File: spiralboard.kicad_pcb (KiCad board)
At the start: 2 copper layers, 88.5 x 100 mm, 85 parts, among them J1 Conn_01x05_Pin, J2 Conn_01x02_Pin, U1 ESP-12F, U2 AMS1117-3.3

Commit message: update
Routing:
- net +3V3: track 96.5 -> 95.2 mm
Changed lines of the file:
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@@
   (segment (start 151.13 133.572) (end 150.654 133.096) (width 0.5) (layer "B.Cu") (net 1))
   (segment (start 176.895 126.619) (end 176.895 126.762) (width 0.5) (layer "B.Cu") (net 1))
-  (segment (start 145.454 124.841) (end 146.304 124.841) (width 0.5) (layer "B.Cu") (net 1))
   (segment (start 176.895 126.619) (end 177.165 126.619) (width 0.5) (layer "B.Cu") (net 1))
   (segment (start 178.816 122.047) (end 172.660918 122.047) (width 0.5) (layer "B.Cu") (net 1))
   (segment (start 150.654 128.365) (end 152.8025 126.2165) (width 0.5) (layer "B.Cu") (net 1))
-  (segment (start 147.182 123.963) (end 147.182 119.761) (width 0.5) (layer "B.Cu") (net 1))
   (segment (start 148.942082 136.486) (end 151.13 134.298082) (width 0.5) (layer "B.Cu") (net 1))
-  (segment (start 147.182 120.534) (end 147.182 119.761) (width 0.5) (layer "B.Cu") (net 1))
-  (segment (start 148.717 116.646864) (end 148.717 113.767) (width 0.5) (layer "B.Cu") (net 1))
   (segment (start 145.454 124.841) (end 145.454 134.972082) (width 0.5) (layer "B.Cu") (net 1))
+  (segment (start 145.454 124.841) (end 146.5795 123.7155) (width 0.5) (layer "B.Cu") (net 1))
   (segment (start 175.26 128.397) (end 175.26 129.286) (width 0.5) (layer "B.Cu") (net 1))
   (segment (start 152.8025 126.2165) (end 152.8025 124.079) (width 0.5) (layer "B.Cu") (net 1))
   (segment (start 152.8025 124.079) (end 155.935 124.079) (width 0.5) (layer "B.Cu") (net 1))
   (segment (start 179.705 124.079) (end 179.705 122.936) (width 0.5) (layer "B.Cu") (net 1))
-  (segment (start 147.182 118.181864) (end 148.717 116.646864) (width 0.5) (layer "B.Cu") (net 1))
   (segment (start 145.454 124.841) (end 143.748 124.841) (width 0.5) (layer "B.Cu") (net 1))
   (segment (start 145.454 134.972082) (end 146.967918 136.486) (width 0.5) (layer "B.Cu") (net 1))
   (segment (start 176.895 130.921) (end 176.895 131.953) (width 0.5) (layer "B.Cu") (net 1))
   (segment (start 150.654 133.096) (end 150.654 128.365) (width 0.5) (layer "B.Cu") (net 1))
+  (segment (start 148.717 116.646864) (end 148.717 113.767) (width 0.5) (layer "B.Cu") (net 1))
+  (segment (start 146.5795 119.761) (end 146.5795 118.784364) (width 0.5) (layer "B.Cu") (net 1))
   (segment (start 175.26 129.286) (end 176.895 130.921) (width 0.5) (layer "B.Cu") (net 1))
   (segment (start 176.895 126.762) (end 175.26 128.397) (width 0.5) (layer "B.Cu") (net 1))
-  (segment (start 146.304 124.841) (end 147.182 123.963) (width 0.5) (layer "B.Cu") (net 1))
   (segment (start 148.717 107.467) (end 148.717 113.767) (width 0.5) (layer "B.Cu") (net 1))
   (segment (start 152.8025 121.92) (end 152.8025 124.079) (width 0.5) (layer "B.Cu") (net 1))
-  (segment (start 147.182 119.761) (end 147.182 118.181864) (width 0.5) (layer "B.Cu") (net 1))
   (segment (start 179.705 122.936) (end 178.816 122.047) (width 0.5) (layer "B.Cu") (net 1))
+  (segment (start 146.5795 123.7155) (end 146.5795 119.761) (width 0.5) (layer "B.Cu") (net 1))
+  (segment (start 146.5795 118.784364) (end 148.717 116.646864) (width 0.5) (layer "B.Cu") (net 1))
   (via (at 181.61 120.396) (size 0.8) (drill 0.4) (layers "F.Cu" "B.Cu") (free) (net 2))
   (via (at 152.527 82.55) (size 0.8) (drill 0.4) (layers "F.Cu" "B.Cu") (free) (net 2))
@@
   (segment (start 156.906 75.504) (end 155.702 76.708) (width 0.5) (layer "F.Cu") (net 3))
   (segment (start 145.303467 115.759607) (end 147.697607 115.759607) (width 0.5) (layer "F.Cu") (net 3))
-  (segment (start 169.093747 112.272253) (end 169.164 112.202) (width 0.5) (layer "F.Cu") (net 3))
   (segment (start 192.404832 84.417916) (end 192.404832 81.849168) (width 0.5) (layer "F.Cu") (net 3))
   (segment (start 158.000249 74.729751) (end 157.226 75.504) (width 0.5) (layer "F.Cu") (net 3))

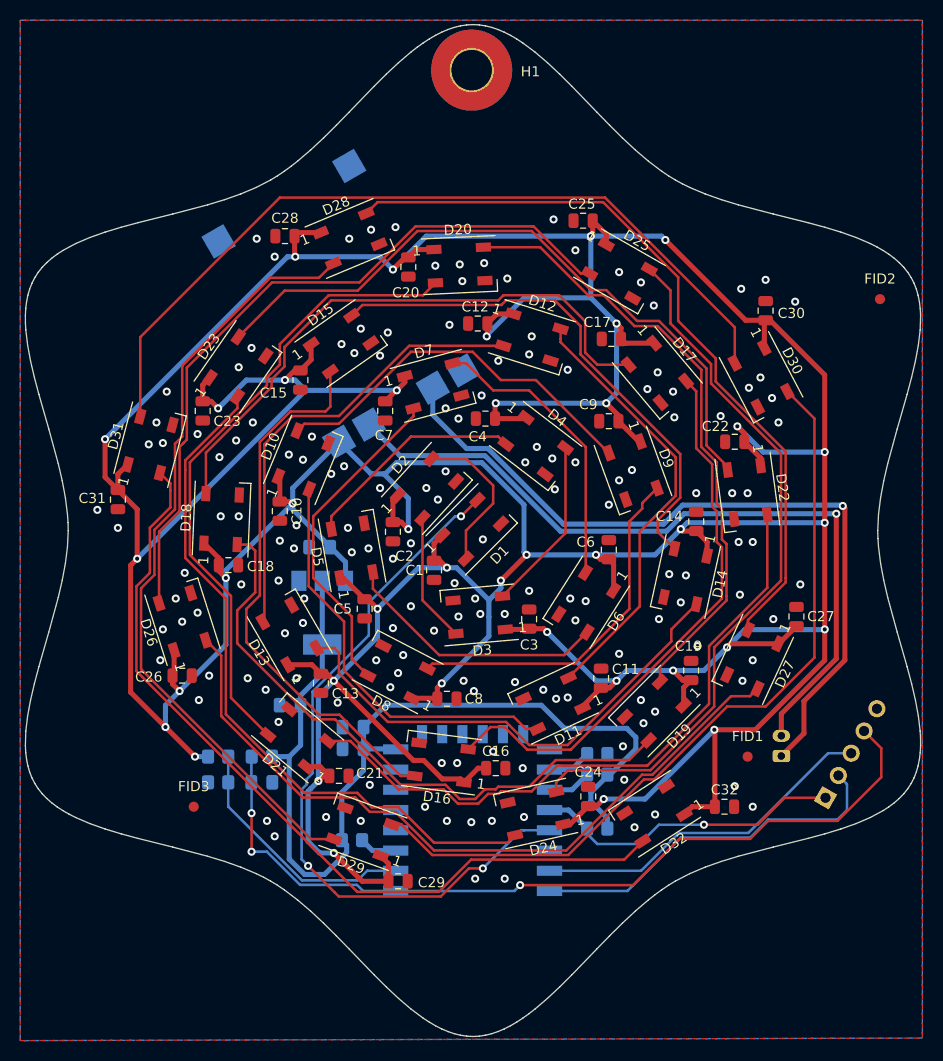
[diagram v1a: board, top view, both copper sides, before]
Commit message: mouting hole vergrößert
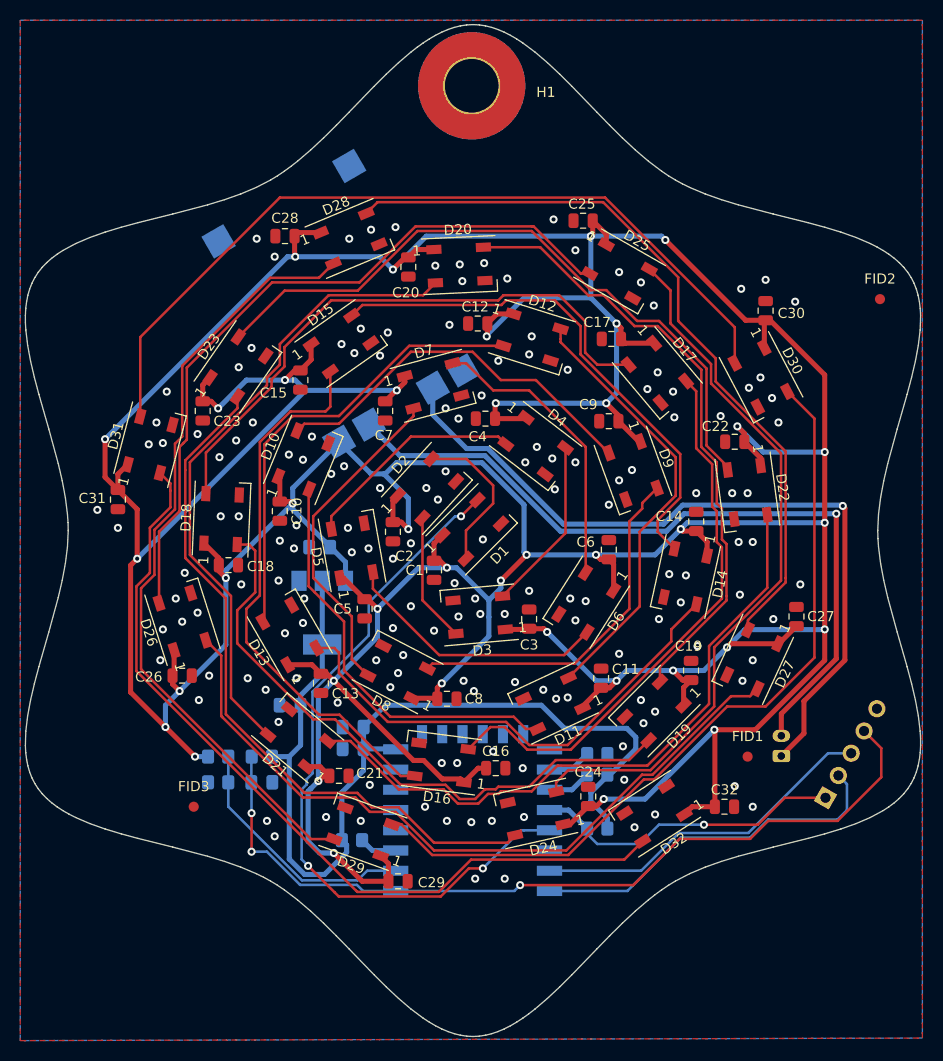
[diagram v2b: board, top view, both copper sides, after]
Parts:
- H1: footprint MountingHole:MountingHole_4mm_Pad_TopBottom -> MountingHole:MountingHole_5.3mm_M5_Pad_TopBottom
- moved H1 1.55 mm to (163.5, 58.5)

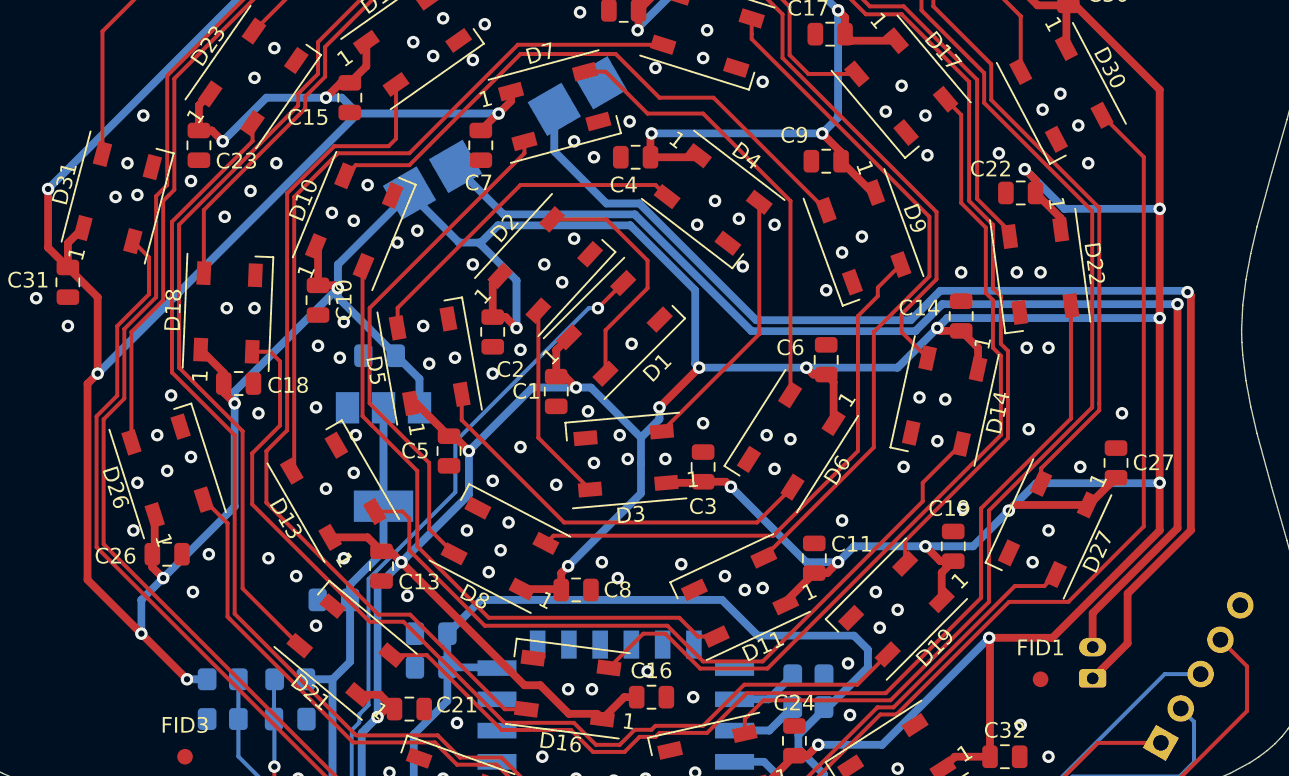
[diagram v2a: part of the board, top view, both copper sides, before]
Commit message: Linearregler getauscht, schalter hinzugefügt
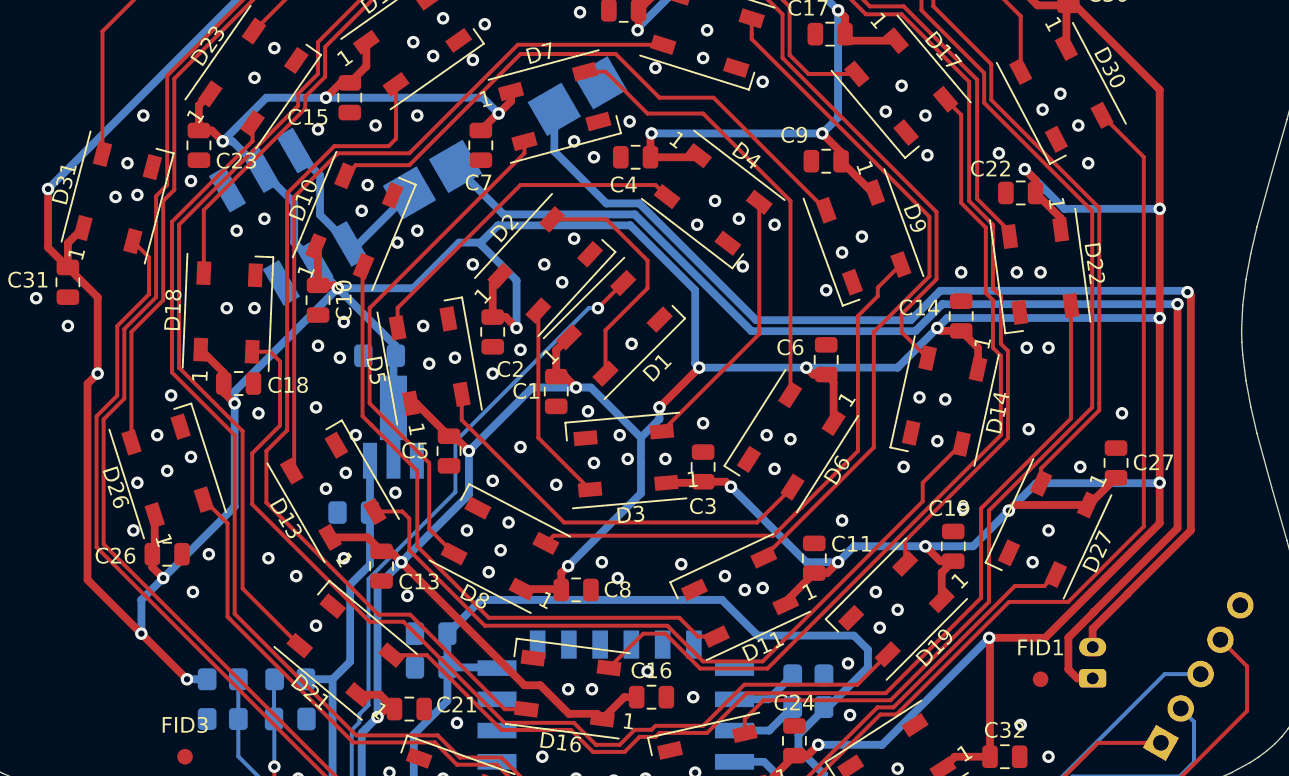
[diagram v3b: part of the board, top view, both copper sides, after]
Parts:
- removed U2: AMS1117-3.3, Package_TO_SOT_SMD:SOT-223-3_TabPin2
- added SW1: SW_DPDT_x2, MSS22D18G2:MSS22D18G2, B.Cu at (142.6, 95.2)
- added U3: ~, Package_TO_SOT_SMD:SOT-89-3_Handsoldering, B.Cu at (149.4, 108.4)
- C36: value 22µF -> 10µF
- moved C36 5.73 mm to (146.8, 114.2)
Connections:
- net EN renamed Net-(U1-EN)
- J2 pad 1: /ESP8266/Bat- -> /ESP8266/Bat+
- J2 pad 2: /ESP8266/Bat+ -> /ESP8266/Bat-
- Mod1 pad 3: VCC -> Net-(Mod1-OUT+)
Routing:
- net Net-(Mod1-OUT+): track 0.00 -> 12.6 mm
- net VCC: track 644.3 -> 632.5 mm
- net /ESP8266/Bat+: track 75.5 -> 79.5 mm
- net +3V3: track 95.2 -> 91.5 mm
- net /ESP8266/Bat-: track 75.9 -> 73.9 mm
- net GND: vias 161 -> 163
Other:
- board text added: "On <-> Off"
